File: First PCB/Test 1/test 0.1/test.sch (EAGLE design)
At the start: 9 parts, among them SW2 B3U-1000P

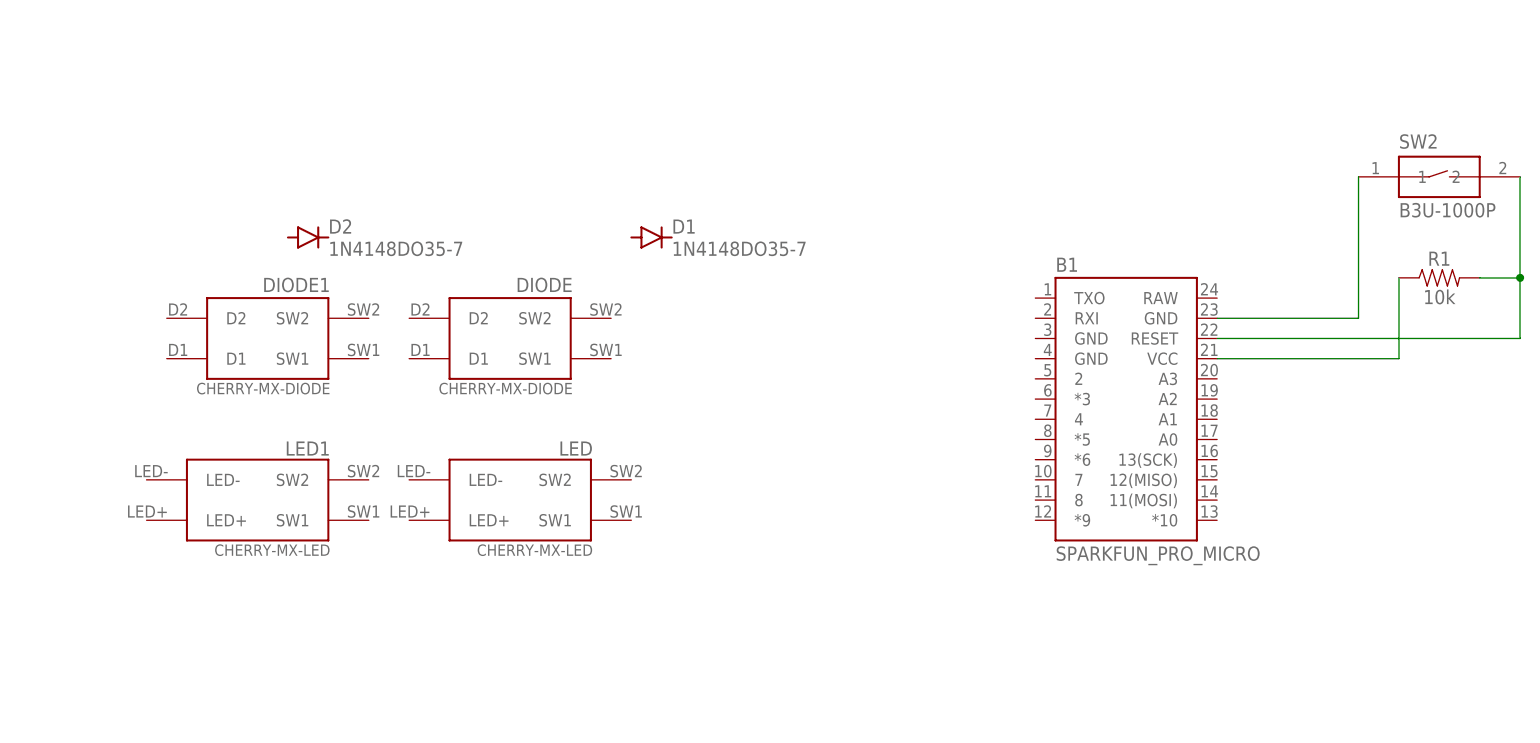
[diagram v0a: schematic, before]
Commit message: added two key switches with diodes
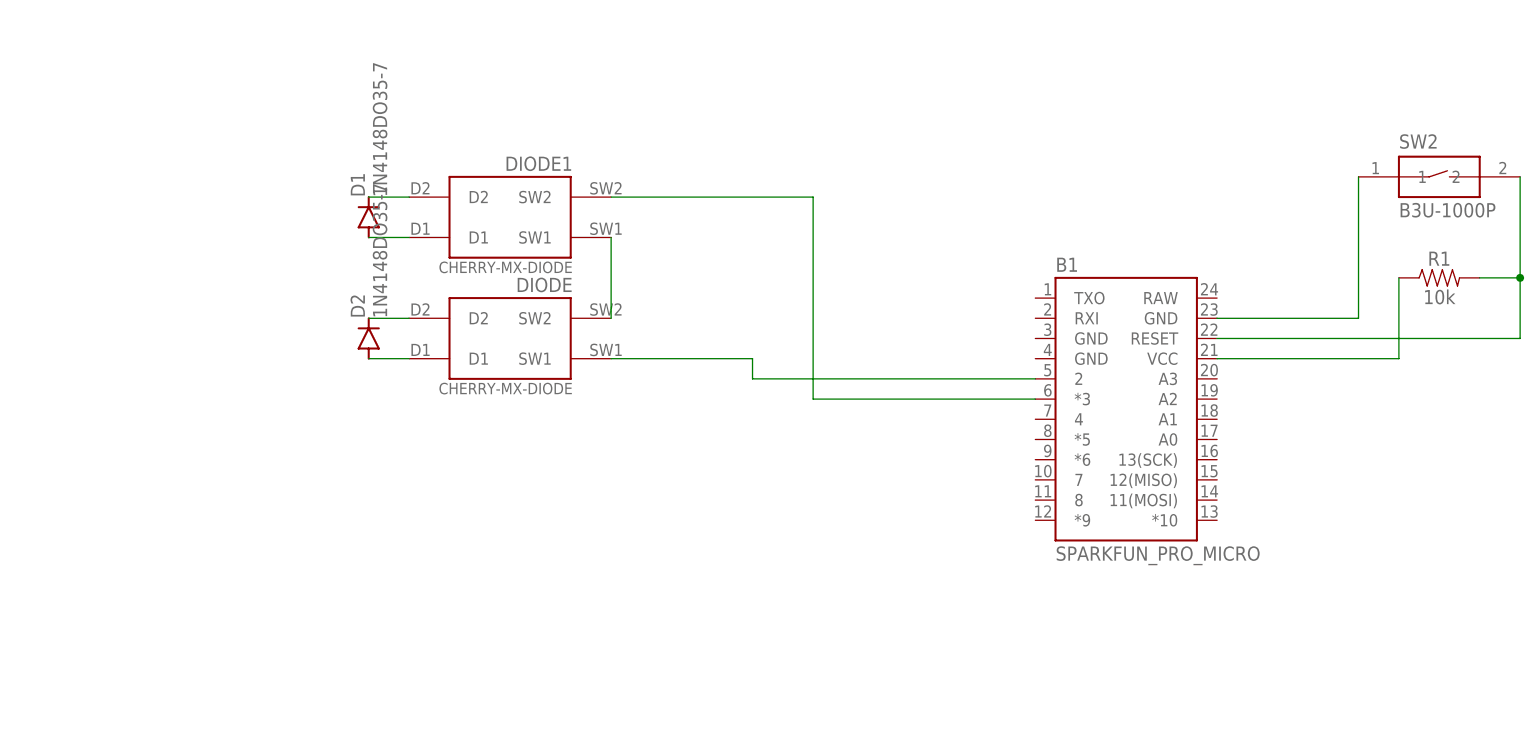
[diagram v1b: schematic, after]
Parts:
- removed LED, LED1: CHERRY-MX-LED, cherrymx:CHERRY-MX-LED
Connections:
- new net N$10: D1.C, DIODE1.D2
- new net N$4: B1.2, DIODE.SW1
- new net N$5: DIODE.SW2, DIODE1.SW1
- new net N$6: B1.*3, DIODE1.SW2
- new net N$7: D2.A, DIODE.D1
- new net N$8: D2.C, DIODE.D2
- new net N$9: D1.A, DIODE1.D1
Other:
- moved on the sheet: D1, D2, DIODE1
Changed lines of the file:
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@@
 <part name="B1" library="SparkFun-Boards" library_urn="urn:adsk.eagle:library:509" deviceset="SPARKFUN_PRO_MICRO" device="" package3d_urn="urn:adsk.eagle:package:37326/1"/>
 <part name="DIODE" library="cherrymx" deviceset="CHERRY-MX-DIODE" device=""/>
-<part name="LED" library="cherrymx" deviceset="CHERRY-MX-LED" device=""/>
 <part name="D1" library="diode" library_urn="urn:adsk.eagle:library:210" deviceset="1N4148" device="DO35-7" package3d_urn="urn:adsk.eagle:package:43339/2"/>
 <part name="DIODE1" library="cherrymx" deviceset="CHERRY-MX-DIODE" device=""/>
-<part name="LED1" library="cherrymx" deviceset="CHERRY-MX-LED" device=""/>
 <part name="D2" library="diode" library_urn="urn:adsk.eagle:library:210" deviceset="1N4148" device="DO35-7" package3d_urn="urn:adsk.eagle:package:43339/2"/>
 <part name="SW2" library="Switch" library_urn="urn:adsk.eagle:library:11396471" deviceset="B3U-1000P" device="" package3d_urn="urn:adsk.eagle:package:10899220/2"/>
@@
 <attribute name="NAME" x="33.274" y="48.26" size="1.778" layer="95" rot="R180"/>
 </instance>
-<instance part="LED" gate="G$1" x="30.48" y="20.32" smashed="yes" rot="R180">
-<attribute name="NAME" x="35.814" y="27.686" size="1.778" layer="95" rot="R180"/>
+<instance part="D1" gate="G$1" x="7.62" y="55.88" smashed="yes" rot="R90">
+<attribute name="NAME" x="7.1374" y="58.42" size="1.778" layer="95" rot="R90"/>
+<attribute name="VALUE" x="9.9314" y="58.42" size="1.778" layer="96" rot="R90"/>
 </instance>
-<instance part="D1" gate="G$1" x="43.18" y="53.34" smashed="yes">
-<attribute name="NAME" x="45.72" y="53.8226" size="1.778" layer="95"/>
-<attribute name="VALUE" x="45.72" y="51.0286" size="1.778" layer="96"/>
+<instance part="DIODE1" gate="G$1" x="27.94" y="55.88" smashed="yes" rot="R180">
+<attribute name="NAME" x="33.274" y="63.5" size="1.778" layer="95" rot="R180"/>
 </instance>
-<instance part="DIODE1" gate="G$1" x="-2.54" y="40.64" smashed="yes" rot="R180">
-<attribute name="NAME" x="2.794" y="48.26" size="1.778" layer="95" rot="R180"/>
-</instance>
-<instance part="LED1" gate="G$1" x="-2.54" y="20.32" smashed="yes" rot="R180">
-<attribute name="NAME" x="2.794" y="27.686" size="1.778" layer="95" rot="R180"/>
-</instance>
-<instance part="D2" gate="G$1" x="0" y="53.34" smashed="yes">
-<attribute name="NAME" x="2.54" y="53.8226" size="1.778" layer="95"/>
-<attribute name="VALUE" x="2.54" y="51.0286" size="1.778" layer="96"/>
+<instance part="D2" gate="G$1" x="7.62" y="40.64" smashed="yes" rot="R90">
+<attribute name="NAME" x="7.1374" y="43.18" size="1.778" layer="95" rot="R90"/>
+<attribute name="VALUE" x="9.9314" y="43.18" size="1.778" layer="96" rot="R90"/>
 </instance>
 <instance part="SW2" gate="G$1" x="142.24" y="60.96" smashed="yes">
@@
 </segment>
 </net>
+<net name="N$5" class="0">
+<segment>
+<pinref part="DIODE1" gate="G$1" pin="SW1"/>
+<pinref part="DIODE" gate="G$1" pin="SW2"/>
+<wire x1="38.1" y1="43.18" x2="38.1" y2="53.34" width="0.1524" layer="91"/>
+</segment>
+</net>
+<net name="N$6" class="0">
+<segment>
+<pinref part="DIODE1" gate="G$1" pin="SW2"/>
+<wire x1="38.1" y1="58.42" x2="63.5" y2="58.42" width="0.1524" layer="91"/>
+<wire x1="63.5" y1="58.42" x2="63.5" y2="33.02" width="0.1524" layer="91"/>
+<pinref part="B1" gate="G$1" pin="*3"/>
+<wire x1="63.5" y1="33.02" x2="91.44" y2="33.02" width="0.1524" layer="91"/>
+</segment>
+</net>
+<net name="N$4" class="0">
+<segment>
+<pinref part="B1" gate="G$1" pin="2"/>
+<wire x1="91.44" y1="35.56" x2="55.88" y2="35.56" width="0.1524" layer="91"/>
+<wire x1="55.88" y1="35.56" x2="55.88" y2="38.1" width="0.1524" layer="91"/>
+<pinref part="DIODE" gate="G$1" pin="SW1"/>
+<wire x1="55.88" y1="38.1" x2="38.1" y2="38.1" width="0.1524" layer="91"/>
+</segment>
+</net>
+<net name="N$7" class="0">
+<segment>
+<pinref part="DIODE" gate="G$1" pin="D1"/>
+<pinref part="D2" gate="G$1" pin="A"/>
+<wire x1="12.7" y1="38.1" x2="7.62" y2="38.1" width="0.1524" layer="91"/>
+</segment>
+</net>
+<net name="N$8" class="0">
+<segment>
+<pinref part="D2" gate="G$1" pin="C"/>
+<pinref part="DIODE" gate="G$1" pin="D2"/>
+<wire x1="7.62" y1="43.18" x2="12.7" y2="43.18" width="0.1524" layer="91"/>
+</segment>
+</net>
+<net name="N$9" class="0">
+<segment>
+<pinref part="DIODE1" gate="G$1" pin="D1"/>
+<pinref part="D1" gate="G$1" pin="A"/>
+<wire x1="12.7" y1="53.34" x2="7.62" y2="53.34" width="0.1524" layer="91"/>
+</segment>
+</net>
+<net name="N$10" class="0">
+<segment>
+<pinref part="DIODE1" gate="G$1" pin="D2"/>
+<pinref part="D1" gate="G$1" pin="C"/>
+<wire x1="12.7" y1="58.42" x2="7.62" y2="58.42" width="0.1524" layer="91"/>
+</segment>
+</net>

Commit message: Finished for the night. Completed board to finished status and added text + qr. Tested upload to oshpark but qr code did not show up.
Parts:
- B1, D1, D2, DIODE, DIODE1: OC_NEWARK (none) -> unknown
- R1: MPN (none) -> MCWR06X1002FTL; OC_NEWARK (none) -> 94X1379
- SW2: OC_NEWARK (none) -> 78M0188
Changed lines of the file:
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@@
 </classes>
 <parts>
-<part name="B1" library="SparkFun-Boards" library_urn="urn:adsk.eagle:library:509" deviceset="SPARKFUN_PRO_MICRO" device="" package3d_urn="urn:adsk.eagle:package:37326/1"/>
-<part name="DIODE" library="cherrymx" deviceset="CHERRY-MX-DIODE" device=""/>
-<part name="D1" library="diode" library_urn="urn:adsk.eagle:library:210" deviceset="1N4148" device="DO35-7" package3d_urn="urn:adsk.eagle:package:43339/2"/>
-<part name="DIODE1" library="cherrymx" deviceset="CHERRY-MX-DIODE" device=""/>
-<part name="D2" library="diode" library_urn="urn:adsk.eagle:library:210" deviceset="1N4148" device="DO35-7" package3d_urn="urn:adsk.eagle:package:43339/2"/>
-<part name="SW2" library="Switch" library_urn="urn:adsk.eagle:library:11396471" deviceset="B3U-1000P" device="" package3d_urn="urn:adsk.eagle:package:10899220/2"/>
-<part name="R1" library="SparkFun-Resistors" deviceset="10KOHM" device="-0402-1/16W-1%" value="10k"/>
+<part name="B1" library="SparkFun-Boards" library_urn="urn:adsk.eagle:library:509" deviceset="SPARKFUN_PRO_MICRO" device="" package3d_urn="urn:adsk.eagle:package:37326/1">
+<attribute name="MF" value=""/>
+<attribute name="MPN" value=""/>
+<attribute name="OC_NEWARK" value="unknown"/>
+</part>
+<part name="DIODE" library="cherrymx" deviceset="CHERRY-MX-DIODE" device="">
+<attribute name="MF" value=""/>
+<attribute name="MPN" value=""/>
+<attribute name="OC_NEWARK" value="unknown"/>
+</part>
+<part name="D1" library="diode" library_urn="urn:adsk.eagle:library:210" deviceset="1N4148" device="DO35-7" package3d_urn="urn:adsk.eagle:package:43339/2">
+<attribute name="MF" value=""/>
+<attribute name="MPN" value=""/>
+<attribute name="OC_NEWARK" value="unknown"/>
+</part>
+<part name="DIODE1" library="cherrymx" deviceset="CHERRY-MX-DIODE" device="">
+<attribute name="MF" value=""/>
+<attribute name="MPN" value=""/>
+<attribute name="OC_NEWARK" value="unknown"/>
+</part>
+<part name="D2" library="diode" library_urn="urn:adsk.eagle:library:210" deviceset="1N4148" device="DO35-7" package3d_urn="urn:adsk.eagle:package:43339/2">
+<attribute name="MF" value=""/>
+<attribute name="MPN" value=""/>
+<attribute name="OC_NEWARK" value="unknown"/>
+</part>
+<part name="SW2" library="Switch" library_urn="urn:adsk.eagle:library:11396471" deviceset="B3U-1000P" device="" package3d_urn="urn:adsk.eagle:package:10899220/2">
+<attribute name="MF" value=""/>
+<attribute name="OC_NEWARK" value="78M0188"/>
+</part>
+<part name="R1" library="SparkFun-Resistors" deviceset="10KOHM" device="-0402-1/16W-1%" value="10k">
+<attribute name="MF" value=""/>
+<attribute name="MPN" value="MCWR06X1002FTL"/>
+<attribute name="OC_NEWARK" value="94X1379"/>
+</part>
 </parts>
 <sheets>
@@
 <attribute name="NAME" x="93.98" y="49.022" size="1.778" layer="95"/>
 <attribute name="VALUE" x="93.98" y="12.7" size="1.778" layer="96"/>
+<attribute name="OC_NEWARK" x="101.6" y="30.48" size="1.778" layer="96" display="off"/>
+<attribute name="MF" x="101.6" y="30.48" size="1.778" layer="96" display="off"/>
+<attribute name="MPN" x="101.6" y="30.48" size="1.778" layer="96" display="off"/>
 </instance>
 <instance part="DIODE" gate="G$1" x="27.94" y="40.64" smashed="yes" rot="R180">
 <attribute name="NAME" x="33.274" y="48.26" size="1.778" layer="95" rot="R180"/>
+<attribute name="OC_NEWARK" x="27.94" y="40.64" size="1.778" layer="96" display="off"/>
+<attribute name="MF" x="27.94" y="40.64" size="1.778" layer="96" display="off"/>
+<attribute name="MPN" x="27.94" y="40.64" size="1.778" layer="96" display="off"/>
 </instance>
 <instance part="D1" gate="G$1" x="7.62" y="55.88" smashed="yes" rot="R90">
 <attribute name="NAME" x="7.1374" y="58.42" size="1.778" layer="95" rot="R90"/>
 <attribute name="VALUE" x="9.9314" y="58.42" size="1.778" layer="96" rot="R90"/>
+<attribute name="OC_NEWARK" x="7.62" y="55.88" size="1.778" layer="96" display="off"/>
+<attribute name="MF" x="7.62" y="55.88" size="1.778" layer="96" display="off"/>
+<attribute name="MPN" x="7.62" y="55.88" size="1.778" layer="96" display="off"/>
 </instance>
 <instance part="DIODE1" gate="G$1" x="27.94" y="55.88" smashed="yes" rot="R180">
 <attribute name="NAME" x="33.274" y="63.5" size="1.778" layer="95" rot="R180"/>
+<attribute name="OC_NEWARK" x="27.94" y="55.88" size="1.778" layer="96" display="off"/>
+<attribute name="MF" x="27.94" y="55.88" size="1.778" layer="96" display="off"/>
+<attribute name="MPN" x="27.94" y="55.88" size="1.778" layer="96" display="off"/>
 </instance>
 <instance part="D2" gate="G$1" x="7.62" y="40.64" smashed="yes" rot="R90">
 <attribute name="NAME" x="7.1374" y="43.18" size="1.778" layer="95" rot="R90"/>
 <attribute name="VALUE" x="9.9314" y="43.18" size="1.778" layer="96" rot="R90"/>
+<attribute name="OC_NEWARK" x="7.62" y="40.64" size="1.778" layer="96" display="off"/>
+<attribute name="MF" x="7.62" y="40.64" size="1.778" layer="96" display="off"/>
+<attribute name="MPN" x="7.62" y="40.64" size="1.778" layer="96" display="off"/>
 </instance>
 <instance part="SW2" gate="G$1" x="142.24" y="60.96" smashed="yes">
 <attribute name="NAME" x="137.16" y="64.516" size="1.778" layer="95"/>
 <attribute name="VALUE" x="137.16" y="55.88" size="1.778" layer="96"/>
+<attribute name="OC_NEWARK" x="142.24" y="60.96" size="1.778" layer="96" display="off"/>
+<attribute name="MF" x="142.24" y="60.96" size="1.778" layer="96" display="off"/>
 </instance>
 <instance part="R1" gate="G$1" x="142.24" y="48.26" smashed="yes">
 <attribute name="NAME" x="142.24" y="49.784" size="1.778" layer="95" font="vector" align="bottom-center"/>
 <attribute name="VALUE" x="142.24" y="46.736" size="1.778" layer="96" font="vector" align="top-center"/>
+<attribute name="OC_NEWARK" x="142.24" y="48.26" size="1.778" layer="96" display="off"/>
+<attribute name="MF" x="142.24" y="48.26" size="1.778" layer="96" display="off"/>
+<attribute name="MPN" x="142.24" y="48.26" size="1.778" layer="96" display="off"/>
 </instance>
 </instances>
